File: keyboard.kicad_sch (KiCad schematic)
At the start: 290 parts, among them J0 USB_C_Receptacle_USB2.0_16P, J1 Conn_ARM_SWD_TagConnect_TC203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, J2 Conn_01x02, Q0 Q_PMOS_GSD, SW0 RotaryEncoder_Switch, SW1 SW_Push, SW10 SW_Push, SW11 SW_Push, SW12 SW_Push, SW13 SW_Push, SW14 SW_Push, SW15 SW_Push, SW16 SW_Push, SW17 SW_Push, SW18 SW_Push, SW19 SW_Push, SW2 SW_Push, SW20 SW_Push, SW21 SW_Push, SW22 SW_Push, SW23 SW_Push, SW24 SW_Push, SW25 SW_Push, SW26 SW_Push, SW27 SW_Push, SW28 SW_Push, SW29 SW_Push, SW3 SW_Push, SW30 SW_Push, SW31 SW_Push, SW32 SW_Push, SW33 SW_Push, SW34 SW_Push, SW35 SW_Push, SW36 SW_Push, SW37 SW_Push, SW38 SW_Push, SW39 SW_Push, SW4 SW_Push, SW40 SW_Push, SW41 SW_Push, SW42 SW_Push, SW43 SW_Push, SW44 SW_Push, SW45 SW_Push, SW46 SW_Push, SW47 SW_Push, SW48 SW_Push, SW49 SW_Push, SW5 SW_Push, SW50 SW_Push, SW51 SW_Push, SW52 SW_Push, SW53 SW_Push, SW54 SW_Push, SW55 SW_Push, SW56 SW_Push, SW57 SW_Push, SW58 SW_Push, SW59 SW_Push, SW6 SW_Push, SW60 SW_Push, SW61 SW_Push, SW62 SW_Push, SW63 SW_Push, SW64 SW_Push, SW65 SW_Push, SW66 SW_Push, SW67 SW_Push, SW68 SW_Push, SW69 SW_Push, SW7 SW_Push, SW70 SW_Push, SW71 SW_Push, SW72 SW_Push, SW73 SW_Push, SW74 SW_Push, SW75 SW_Push, SW76 SW_Push, SW77 SW_Push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

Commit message: routing
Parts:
- added Q1: Q_PMOS_GSD, Package_TO_SOT_SMD:SOT-23, symbol Device:Q_PMOS_GSD
- added R11: 100k, Resistor_SMD:R_0603_1608Metric, symbol Device:R
- added R12: 10k, Resistor_SMD:R_0603_1608Metric, symbol Device:R
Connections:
- net COL11: now also SW81.2
- net COL12: no longer SW81.2
- net COL13: now also SW77.2, SW82.2, SW87.2
- net COL14: no longer SW77.2, SW82.2, SW87.2
- net VCC: now also Q1.2 (S), R11.2; no longer LED0.4 (VDD), LED1.4 (VDD), LED10.4 (VDD), LED11.4 (VDD), LED12.4 (VDD), LED13.4 (VDD), LED14.4 (VDD), LED15.4 (VDD), LED16.4 (VDD), LED17.4 (VDD), LED18.4 (VDD), LED19.4 (VDD), LED2.4 (VDD), LED20.4 (VDD), LED21.4 (VDD), LED22.4 (VDD), LED23.4 (VDD), LED24.4 (VDD), LED25.4 (VDD), LED26.4 (VDD), LED27.4 (VDD), LED28.4 (VDD), LED29.4 (VDD), LED3.4 (VDD), LED30.4 (VDD), LED31.4 (VDD), LED32.4 (VDD), LED33.4 (VDD), LED34.4 (VDD), LED35.4 (VDD), LED36.4 (VDD), LED37.4 (VDD), LED38.4 (VDD), LED39.4 (VDD), LED4.4 (VDD), LED40.4 (VDD), LED41.4 (VDD), LED42.4 (VDD), LED43.4 (VDD), LED44.4 (VDD), LED45.4 (VDD), LED46.4 (VDD), LED47.4 (VDD), LED48.4 (VDD), LED49.4 (VDD), LED5.4 (VDD), LED50.4 (VDD), LED51.4 (VDD), LED52.4 (VDD), LED53.4 (VDD), LED54.4 (VDD), LED55.4 (VDD), LED56.4 (VDD), LED57.4 (VDD), LED58.4 (VDD), LED59.4 (VDD), LED6.4 (VDD), LED60.4 (VDD), LED61.4 (VDD), LED62.4 (VDD), LED63.4 (VDD), LED64.4 (VDD), LED65.4 (VDD), LED66.4 (VDD), LED67.4 (VDD), LED68.4 (VDD), LED69.4 (VDD), LED7.4 (VDD), LED70.4 (VDD), LED71.4 (VDD), LED72.4 (VDD), LED73.4 (VDD), LED74.4 (VDD), LED8.4 (VDD), LED9.4 (VDD)
- new net: Q1.1 (G), R11.1, R12.1
- new net LED_EN: R12.2
- new net VCC_LED: LED0.4 (VDD), LED1.4 (VDD), LED10.4 (VDD), LED11.4 (VDD), LED12.4 (VDD), LED13.4 (VDD), LED14.4 (VDD), LED15.4 (VDD), LED16.4 (VDD), LED17.4 (VDD), LED18.4 (VDD), LED19.4 (VDD), LED2.4 (VDD), LED20.4 (VDD), LED21.4 (VDD), LED22.4 (VDD), LED23.4 (VDD), LED24.4 (VDD), LED25.4 (VDD), LED26.4 (VDD), LED27.4 (VDD), LED28.4 (VDD), LED29.4 (VDD), LED3.4 (VDD), LED30.4 (VDD), LED31.4 (VDD), LED32.4 (VDD), LED33.4 (VDD), LED34.4 (VDD), LED35.4 (VDD), LED36.4 (VDD), LED37.4 (VDD), LED38.4 (VDD), LED39.4 (VDD), LED4.4 (VDD), LED40.4 (VDD), LED41.4 (VDD), LED42.4 (VDD), LED43.4 (VDD), LED44.4 (VDD), LED45.4 (VDD), LED46.4 (VDD), LED47.4 (VDD), LED48.4 (VDD), LED49.4 (VDD), LED5.4 (VDD), LED50.4 (VDD), LED51.4 (VDD), LED52.4 (VDD), LED53.4 (VDD), LED54.4 (VDD), LED55.4 (VDD), LED56.4 (VDD), LED57.4 (VDD), LED58.4 (VDD), LED59.4 (VDD), LED6.4 (VDD), LED60.4 (VDD), LED61.4 (VDD), LED62.4 (VDD), LED63.4 (VDD), LED64.4 (VDD), LED65.4 (VDD), LED66.4 (VDD), LED67.4 (VDD), LED68.4 (VDD), LED69.4 (VDD), LED7.4 (VDD), LED70.4 (VDD), LED71.4 (VDD), LED72.4 (VDD), LED73.4 (VDD), LED74.4 (VDD), LED8.4 (VDD), LED9.4 (VDD), Q1.3 (D)

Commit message: First finished routing, to check and tune
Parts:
- removed C10, C9: 12pF, Capacitor_SMD:C_0402_1005Metric, symbol Device:C
- removed Y1: Crystal, Crystal:Resonator_SMD_Murata_CSTxExxV-3Pin_3.0x1.1mm, symbol Device:Crystal_GND2
- added D77: 1N4148WT, Diode_SMD:D_SOD-523, symbol Device:D
- added R13, R14: 10k, Resistor_SMD:R_0603_1608Metric, symbol Device:R
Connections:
- net XL- is gone; now on net COL10: U0.F2 (XL2/P0.01)
- net BATP: now also J2.2 (Pin_2), R13.1; no longer J2.1 (Pin_1)
- net COL0: now also U0.AD18 (P0.22)
- net COL1: now also U0.J24 (NFC2/P0.10)
- net COL11: now also U0.G1 (P0.26)
- net COL12: now also U0.L1 (P0.06)
- net COL13: now also U0.N1 (P0.08)
- net COL14: now also U0.R1 (TRACEDATA3/P1.09)
- net COL2: now also U0.U1 (TRACEDATA1/P0.12)
- net COL3: now also U0.B19 (P1.11)
- net COL4: now also U0.A20 (P1.10)
- net COL5: now also U0.A16 (P1.13)
- net COL6: now also U0.A14 (P1.15)
- net COL7: now also U0.A12 (AIN0/P0.02)
- net COL8: now also U0.A10 (AIN5/P0.29)
- net COL9: now also U0.A8 (AIN7/P0.31)
- net ENC_A: now also U0.R24 (P1.06)
- net ENC_B: now also U0.U24 (P1.04)
- net GND: now also J2.1 (Pin_1), R14.2; no longer AE0.2 (Shield), J2.2 (Pin_2)
- net LED_D: now also J1.3 (~{RESET}), U0.AC13 (P0.18/~{RESET})
- net LED_EN: now also U0.AD8 (P0.13)
- net ROW0: now also U0.L24 (NFC1/P0.09)
- net ROW1: now also U0.AD10 (P0.15)
- net ROW2: now also U0.AD20 (P0.24)
- net ROW3: now also U0.AD22 (TRACEDATA0/P1.00)
- net ROW4: now also U0.W24 (P1.02)
- net VDD: now also J1.1 (VCC)
- net BATP_SENSE: now reaches U0.J1 (AIN2/P0.04)
- net BATP_SENSE: now also R13.2, R14.1
- net XL+: no longer names the net of U0.D2 (XL1/P0.00)
- no-connect marks 6 -> 7
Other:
- note added: "Not On Board"
- moved on the sheet: C2, C3, R9, U1

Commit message: Routing fix
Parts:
- removed D77: 1N4148WT, Diode_SMD:D_SOD-523, symbol Device:D
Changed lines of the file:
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@@
 	)
 	(symbol
-		(lib_id "Device:D")
-		(at 383.54 93.98 90)
-		(unit 1)
-		(exclude_from_sim no)
-		(in_bom yes)
-		(on_board yes)
-		(dnp no)
-		(fields_autoplaced yes)
-		(property "Reference" "D77"
-			(at 386.08 92.71 90)
-			(effects
-				(font
-					(size 1.27 1.27)
-				)
-				(justify right)
-			)
-		)
-		(property "Value" "1N4148WT"
-			(at 386.08 95.25 90)
-			(effects
-				(font
-					(size 1.27 1.27)
-				)
-				(justify right)
-			)
-		)
-		(property "Footprint" "Diode_SMD:D_SOD-523"
-			(at 383.54 93.98 0)
-			(effects
-				(font
-					(size 1.27 1.27)
-				)
-				(hide yes)
-			)
-		)
-		(property "Datasheet" "~"
-			(at 383.54 93.98 0)
-			(effects
-				(font
-					(size 1.27 1.27)
-				)
-				(hide yes)
-			)
-		)
-		(property "Description" ""
-			(at 383.54 93.98 0)
-			(effects
-				(font
-					(size 1.27 1.27)
-				)
-				(hide yes)
-			)
-		)
-		(property "Sim.Device" "D"
-			(at 383.54 93.98 0)
-			(effects
-				(font
-					(size 1.27 1.27)
-				)
-				(hide yes)
-			)
-		)
-		(property "Sim.Pins" "1=K 2=A"
-			(at 383.54 93.98 0)
-			(effects
-				(font
-					(size 1.27 1.27)
-				)
-				(hide yes)
-			)
-		)
-		(pin "2"
-		)
-		(pin "1"
-		)
-		(instances
-			(project "keyboard"
-				(path "/036bed95-285c-41d7-ae9e-209431e9628a"
-					(reference "D77")
-					(unit 1)
-				)
-			)
-		)
-	)
-	(symbol
 		(lib_id "Switch:SW_Push")
 		(at 330.2 226.06 0)
@@
 		(exclude_from_sim no)
 		(in_bom yes)
-		(on_board yes)
+		(on_board no)
 		(dnp no)
 		(fields_autoplaced yes)

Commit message: Review version, mechanical started
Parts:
- added H0, H1, H2, H3, H4, H5, H7, H8, H9: MountingHole, MountingHole:MountingHole_2.7mm_M2.5_ISO7380, symbol Mechanical:MountingHole
- J0: footprint Volpx:TYPE-C-31-M-14 -> Volpx:Molex_USBC_2169900001
- SW1, SW10, SW11, SW12, SW17, SW18, SW19, SW2, SW20, SW21, SW22, SW23, SW24, SW25, SW26, SW27, SW3, SW32, SW33, SW34, SW35, SW36, SW37, SW38, SW39, SW4, SW40, SW41, SW42, SW47, SW48, SW49, SW5, SW50, SW51, SW52, SW53, SW54, SW55, SW56, SW57, SW58, SW59, SW6, SW60, SW61, SW62, SW63, SW68, SW69, SW7, SW70, SW71, SW72, SW73, SW74, SW75, SW76, SW77, SW79, SW8, SW80, SW82, SW83, SW87, SW9: footprint Volpx:SW_mechanical_many_v2 -> Volpx:SW_mechanical_many_v2_MovedCuts
- SW13, SW14, SW15, SW16, SW28, SW29, SW30, SW31, SW43, SW44, SW45, SW46, SW64, SW65, SW66, SW67, SW78, SW81, SW84: footprint Volpx:SW_mechanical_many_v2 -> Volpx:SW_mechanical_many_v2_MovedCuts; now not fitted

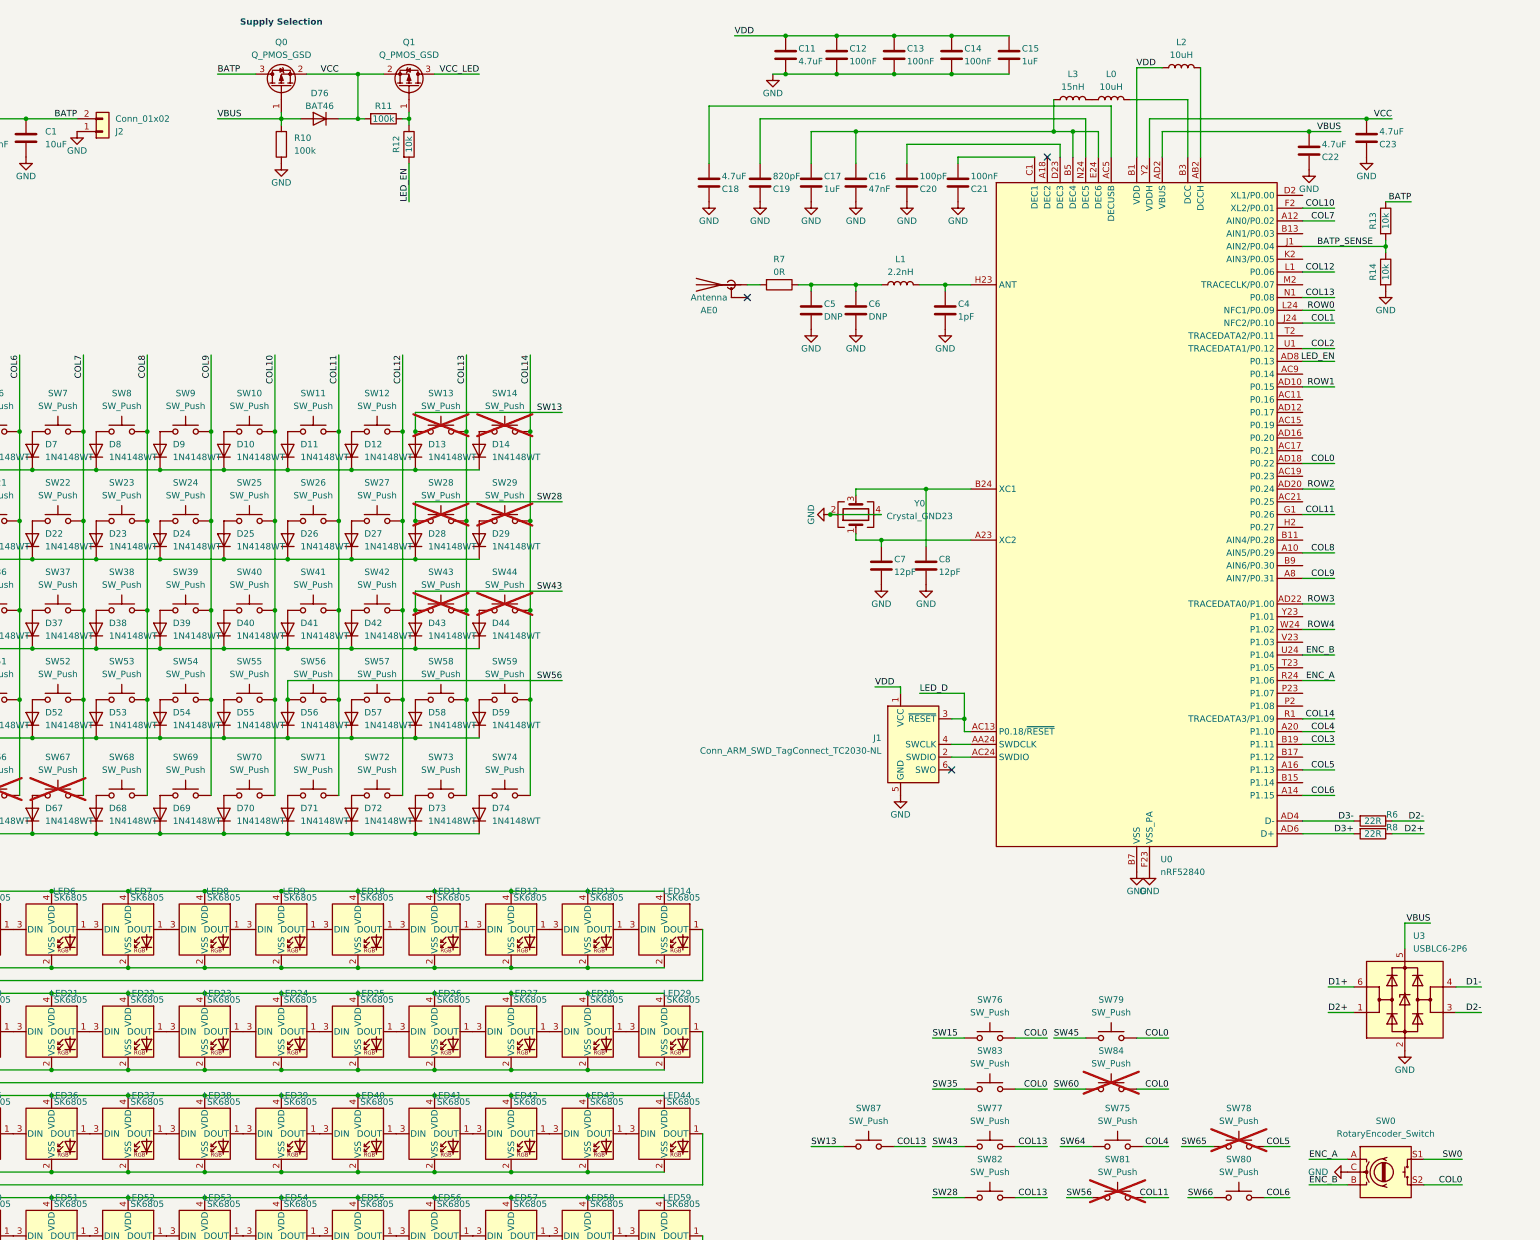
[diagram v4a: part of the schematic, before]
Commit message: Changed project name
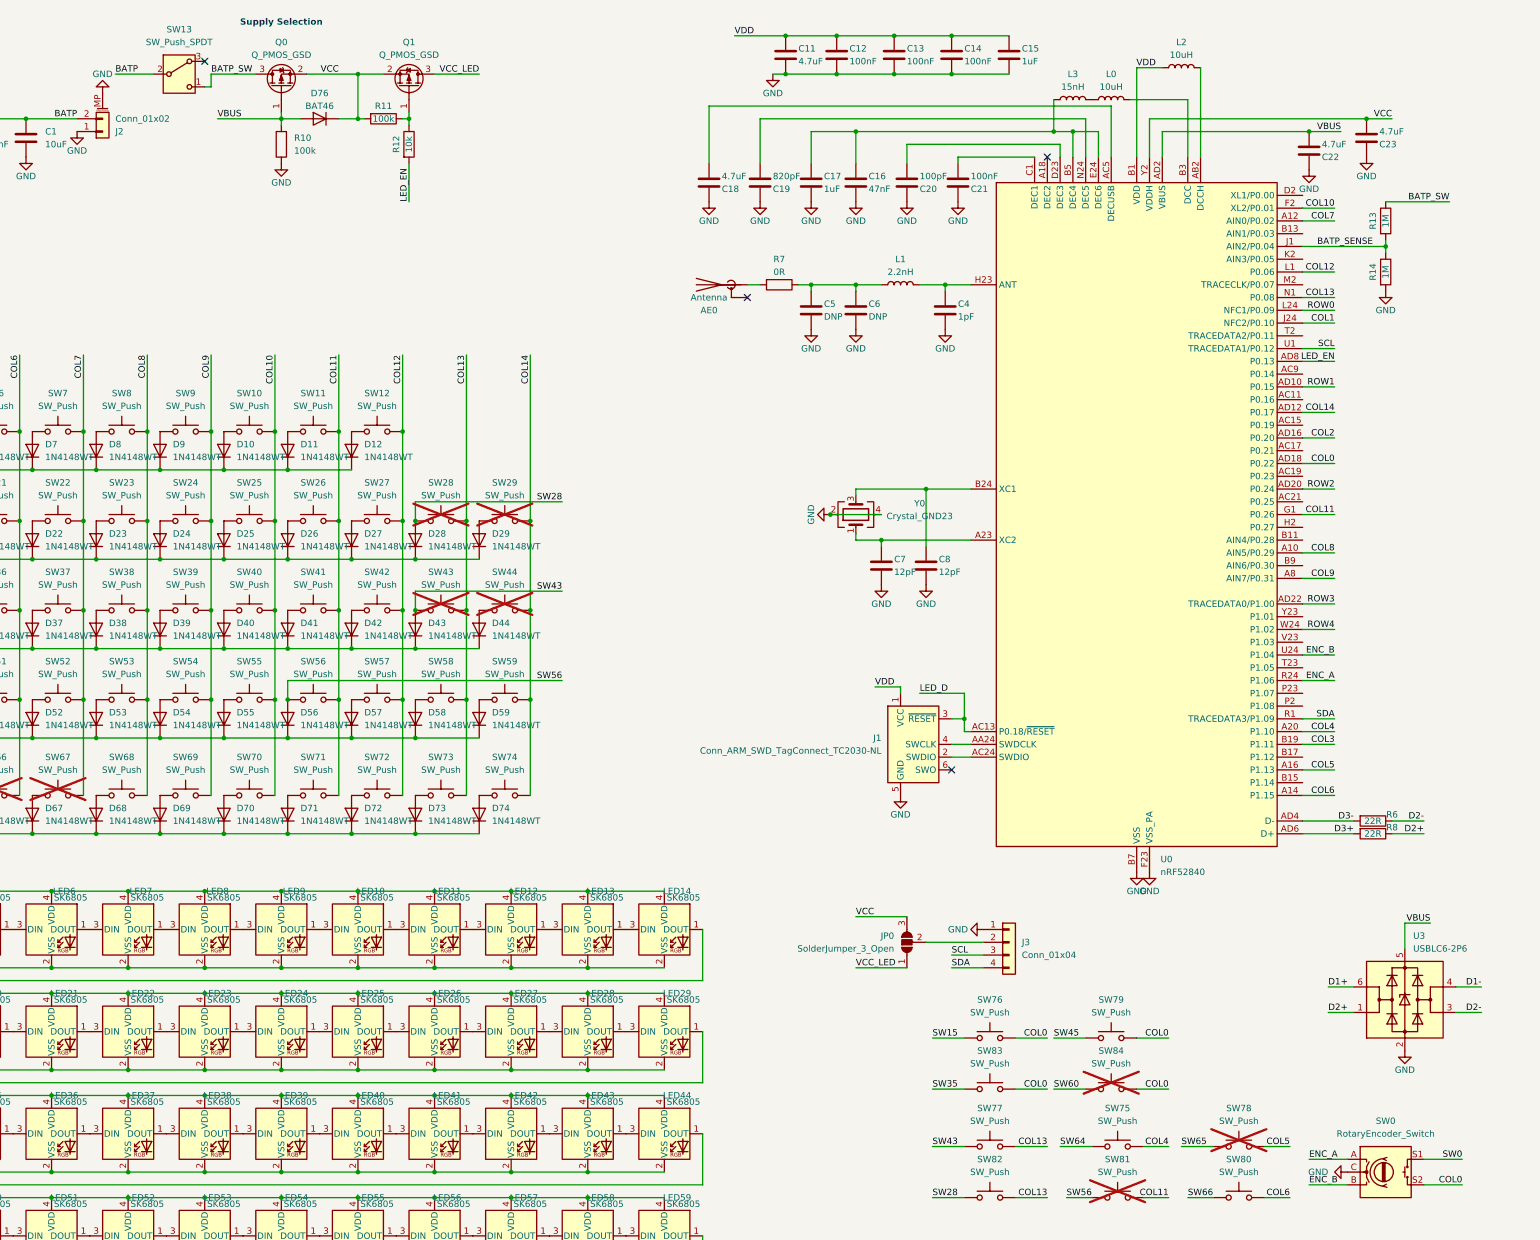
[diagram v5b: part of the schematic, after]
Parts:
- removed D13, D14: 1N4148WT, Diode_SMD:D_SOD-523, symbol Device:D
- removed SW13, SW14, SW87: SW_Push, Volpx:SW_mechanical_many_v2_MovedCuts, symbol Switch:SW_Push
- added J3: Conn_01x04, Volpx:SSD1306-0.91-OLED-4pin-128x32, symbol Connector_Generic:Conn_01x04
- added JP0: SolderJumper_3_Open, Jumper:SolderJumper-3_P1.3mm_Open_RoundedPad1.0x1.5mm_NumberLabels, symbol Jumper:SolderJumper_3_Open
- added SW13: SW_Push_SPDT, Button_Switch_THT:SW_Slide-03_Wuerth-WS-SLTV_10x2.5x6.4_P2.54mm, symbol Switch:SW_SPDT_321
- J2: symbol Connector_Generic:Conn_01x02 -> Connector_Generic_MountingPin:Conn_01x02_MountingPin
- R13, R14: value 10k -> 1M
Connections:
- net BATP: now also SW13.2 (B); no longer Q0.3 (D), R13.1
- net COL14: now also U0.AD12 (P0.17); no longer U0.R1 (TRACEDATA3/P1.09)
- net COL2: now also U0.AD16 (P0.20); no longer U0.U1 (TRACEDATA1/P0.12)
- net GND: now also J2.MP (MountPin), J3.1 (Pin_1)
- net VCC: now also JP0.3 (B)
- net VCC_LED: now also JP0.1 (A)
- new net: J3.2 (Pin_2), JP0.2 (C)
- new net BATP_SW: Q0.3 (D), R13.1, SW13.1 (C)
- new net SCL: J3.3 (Pin_3), U0.U1 (TRACEDATA1/P0.12)
- new net SDA: J3.4 (Pin_4), U0.R1 (TRACEDATA3/P1.09)
- no-connect marks 7 -> 8
